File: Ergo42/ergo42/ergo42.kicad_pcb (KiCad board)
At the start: 2 copper layers, 135.9 x 102.2 mm, 97 parts, among them J1 , J3 , J4 , SW1 , SW17 , SW18 , SW19 , SW20 , SW21 , SW22 , SW23 , SW3 , SW31 , SW32 , SW33 , SW34 , SW35 , SW36 , SW37 , SW4 , SW45 , SW46 , SW47 , SW48 , SW49 , SW5 , SW50 , SW51 , SW6 , SW7 , SW8 , SW9 , U1 ProMicro, p1 PJ-320

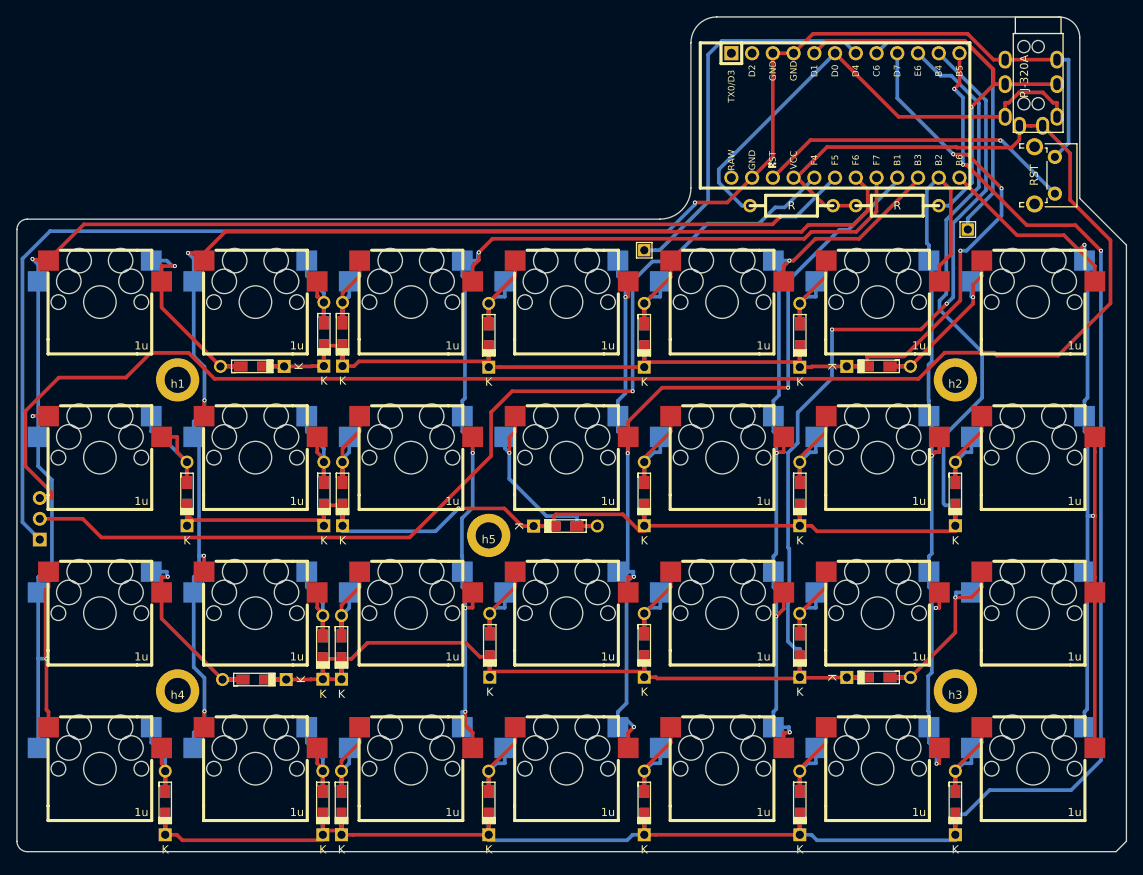
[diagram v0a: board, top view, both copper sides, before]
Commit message: add some keyboard
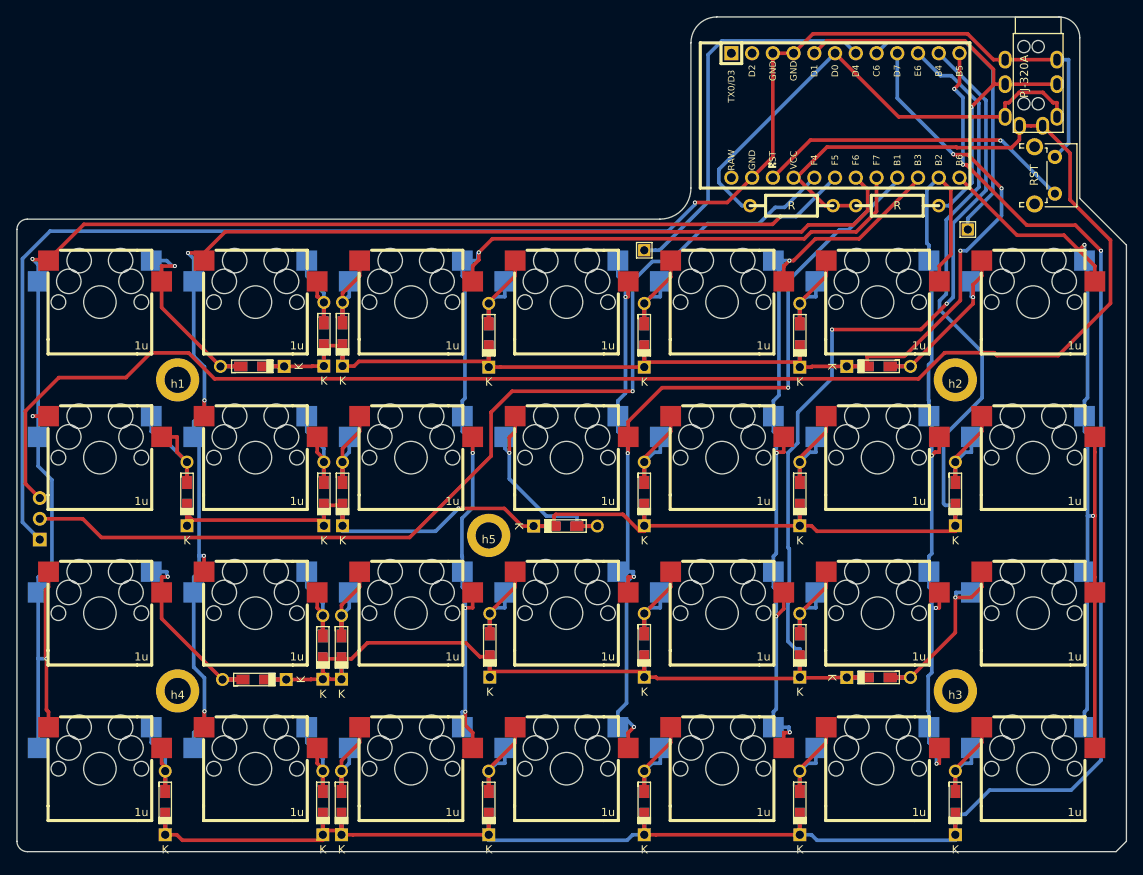
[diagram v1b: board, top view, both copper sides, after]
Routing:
- net +5V: track 222.8 -> 220.8 mm
